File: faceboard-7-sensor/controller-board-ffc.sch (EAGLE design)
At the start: 8 parts, among them J1 DCJ0202

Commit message: redraw schematics
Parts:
- removed FACEBOARD: 52806-1410, 52806-1410:52806-1410
- RIBBON1: value 686114148922 -> (none)
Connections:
- net FRAM_CLK renamed CLK
- net FRAM_CS renamed CS
- net FRAM_MISO renamed MISO
- net FRAM_MOSI renamed MOSI
- net ROTA renamed RA
- net ROTB renamed RB
- net ROTC renamed RC
- removed net 5V: FACEBOARD.3, J1.1, RIBBON1.3, U$1.RAW
- removed net A4: FACEBOARD.12, RIBBON1.12, U$1.A4
- removed net A6: FACEBOARD.14, RIBBON1.14, U$1.A6
- removed net A7: U$1.A7
- removed net AREF: U$1.AREF
- removed net D0: U$1.TX0
- removed net D1: U$1.RX1
- removed net D13: U$1.D13
- removed net LEDDATA: FACEBOARD.7, LEDR.2, RIBBON1.7
- removed net N$8: FRAM.1
- removed net NC3V: FRAM.7
- removed net RST0: U$1.RST
- removed net VUSB: U$1.5.5V
- new net DIN: LEDR.2, RIBBON1.7
- new net N$1: RIBBON1.12, U$1.A4
- new net N$2: RIBBON1.14, U$1.A6
- new net VCC: J1.1, RIBBON1.3, U$1.RAW
- net 3V: no longer FACEBOARD.2
- net A: no longer FACEBOARD.4
- net A0: no longer FACEBOARD.8
- net A1: no longer FACEBOARD.9
- net A2: no longer FACEBOARD.10
- net A3: no longer FACEBOARD.11
- net A5: no longer FACEBOARD.13
- net B: no longer FACEBOARD.5
- net C: no longer FACEBOARD.6
- net GND: no longer FACEBOARD.1
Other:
- moved on the sheet: FRAM, J1, RESET, ROTARY

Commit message: reroute
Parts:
- RIBBON1: value (none) -> Signal
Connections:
- net N$1 renamed A4
- net N$2 renamed A6
- net A: now also U$1.D8; no longer U$1.D6
- net C: now also U$1.D6; no longer U$1.D8
- net GND: now also FRAM.7; no longer FRAM.6
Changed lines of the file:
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@@
 <part name="LEDR" library="rcl" library_urn="urn:adsk.eagle:library:334" deviceset="R-EU_" device="0207/10" package3d_urn="urn:adsk.eagle:package:23491/2" value="300"/>
 <part name="FRAM" library="con-lstb" library_urn="urn:adsk.eagle:library:162" deviceset="MA08-1" device="" package3d_urn="urn:adsk.eagle:package:8343/1" value="MB85RS2MTA"/>
-<part name="RIBBON1" library="686114148922" deviceset="686114148922" device=""/>
+<part name="RIBBON1" library="686114148922" deviceset="686114148922" device="" value="Signal"/>
 <part name="J1" library="con-jack" library_urn="urn:adsk.eagle:library:154" deviceset="DCJ0202" device="" package3d_urn="urn:adsk.eagle:package:7491/1"/>
 <part name="RESET" library="con-jst-ph" deviceset="B2B-PH-K" device=""/>
@@
 <pinref part="RIBBON1" gate="G$1" pin="13"/>
 <wire x1="38.1" y1="53.34" x2="17.018" y2="53.34" width="0.1524" layer="91"/>
+<label x="22.86" y="53.34" size="1.778" layer="95"/>
 </segment>
 </net>
@@
 </segment>
 </net>
-<net name="A0" class="0">
-<segment>
-<pinref part="U$1" gate="G$1" pin="A0"/>
-<wire x1="17.018" y1="66.04" x2="38.1" y2="66.04" width="0.1524" layer="91"/>
-<wire x1="17.018" y1="66.04" x2="17.272" y2="66.04" width="0.1524" layer="91"/>
-<pinref part="RIBBON1" gate="G$1" pin="8"/>
-</segment>
-</net>
 <net name="A" class="0">
+<segment>
+<wire x1="17.018" y1="76.2" x2="17.272" y2="76.2" width="0.1524" layer="91"/>
+<label x="17.272" y="76.2" size="1.778" layer="95" xref="yes"/>
+<pinref part="RIBBON1" gate="G$1" pin="4"/>
+</segment>
+<segment>
+<pinref part="U$1" gate="G$1" pin="D8"/>
+<wire x1="71.12" y1="63.5" x2="71.628" y2="63.5" width="0.1524" layer="91"/>
+<label x="75.692" y="63.5" size="1.778" layer="95" rot="MR0" xref="yes"/>
+</segment>
+</net>
+<net name="B" class="0">
+<segment>
+<pinref part="U$1" gate="G$1" pin="D7"/>
+<wire x1="75.692" y1="60.96" x2="71.12" y2="60.96" width="0.1524" layer="91"/>
+<label x="79.756" y="60.96" size="1.778" layer="95" rot="MR0" xref="yes"/>
+</segment>
+<segment>
+<wire x1="17.018" y1="73.66" x2="22.352" y2="73.66" width="0.1524" layer="91"/>
+<label x="22.352" y="73.66" size="1.778" layer="95" xref="yes"/>
+<pinref part="RIBBON1" gate="G$1" pin="5"/>
+</segment>
+</net>
+<net name="C" class="0">
+<segment>
+<wire x1="17.018" y1="71.12" x2="17.272" y2="71.12" width="0.1524" layer="91"/>
+<label x="17.272" y="71.12" size="1.778" layer="95" xref="yes"/>
+<pinref part="RIBBON1" gate="G$1" pin="6"/>
+</segment>
 <segment>
 <pinref part="U$1" gate="G$1" pin="D6"/>
@@
 <label x="75.438" y="58.42" size="1.778" layer="95" rot="MR0" xref="yes"/>
 </segment>
-<segment>
-<wire x1="17.018" y1="76.2" x2="17.272" y2="76.2" width="0.1524" layer="91"/>
-<label x="17.272" y="76.2" size="1.778" layer="95" xref="yes"/>
-<pinref part="RIBBON1" gate="G$1" pin="4"/>
-</segment>
-</net>
-<net name="B" class="0">
-<segment>
-<pinref part="U$1" gate="G$1" pin="D7"/>
-<wire x1="75.692" y1="60.96" x2="71.12" y2="60.96" width="0.1524" layer="91"/>
-<label x="79.756" y="60.96" size="1.778" layer="95" rot="MR0" xref="yes"/>
-</segment>
-<segment>
-<wire x1="17.018" y1="73.66" x2="22.352" y2="73.66" width="0.1524" layer="91"/>
-<label x="22.352" y="73.66" size="1.778" layer="95" xref="yes"/>
-<pinref part="RIBBON1" gate="G$1" pin="5"/>
-</segment>
-</net>
-<net name="C" class="0">
-<segment>
-<pinref part="U$1" gate="G$1" pin="D8"/>
-<wire x1="71.12" y1="63.5" x2="71.628" y2="63.5" width="0.1524" layer="91"/>
-<label x="75.692" y="63.5" size="1.778" layer="95" rot="MR0" xref="yes"/>
-</segment>
-<segment>
-<wire x1="17.018" y1="71.12" x2="17.272" y2="71.12" width="0.1524" layer="91"/>
-<label x="17.272" y="71.12" size="1.778" layer="95" xref="yes"/>
-<pinref part="RIBBON1" gate="G$1" pin="6"/>
-</segment>
 </net>
 <net name="RST" class="0">
@@
 <wire x1="39.37" y1="4.064" x2="32.766" y2="4.064" width="0.1524" layer="91"/>
 <label x="32.766" y="4.064" size="1.778" layer="95" rot="R180" xref="yes"/>
-</segment>
-<segment>
-<wire x1="69.85" y1="9.906" x2="70.104" y2="9.906" width="0.1524" layer="91"/>
-<pinref part="FRAM" gate="1" pin="6"/>
-<label x="70.104" y="9.906" size="1.778" layer="95" rot="MR180" xref="yes"/>
 </segment>
 <segment>
@@
 <wire x1="27.94" y1="43.18" x2="27.94" y2="40.64" width="0.1524" layer="91"/>
 <junction x="27.94" y="40.64"/>
+<label x="33.02" y="40.64" size="1.778" layer="95" rot="R90" xref="yes"/>
+</segment>
+<segment>
+<pinref part="FRAM" gate="1" pin="7"/>
+<wire x1="69.85" y1="7.366" x2="76.2" y2="7.366" width="0.1524" layer="91"/>
+<label x="76.454" y="7.366" size="1.778" layer="95" xref="yes"/>
 </segment>
 </net>
@@
 </segment>
 </net>
-<net name="N$1" class="0">
+<net name="A4" class="0">
 <segment>
 <pinref part="U$1" gate="G$1" pin="A4"/>
 <pinref part="RIBBON1" gate="G$1" pin="12"/>
 <wire x1="38.1" y1="55.88" x2="17.018" y2="55.88" width="0.1524" layer="91"/>
-</segment>
-</net>
-<net name="N$2" class="0">
+<label x="22.86" y="55.88" size="1.778" layer="95"/>
+</segment>
+</net>
+<net name="A6" class="0">
 <segment>
 <pinref part="U$1" gate="G$1" pin="A6"/>
 <pinref part="RIBBON1" gate="G$1" pin="14"/>
 <wire x1="38.1" y1="50.8" x2="17.018" y2="50.8" width="0.1524" layer="91"/>
-</segment>
-</net>
+<label x="22.86" y="50.8" size="1.778" layer="95"/>
+</segment>
+</net>
+<net name="A0" class="0">
+<segment>
+<pinref part="RIBBON1" gate="G$1" pin="8"/>
+<pinref part="U$1" gate="G$1" pin="A0"/>
+<wire x1="17.018" y1="66.04" x2="38.1" y2="66.04" width="0.1524" layer="91"/>
+<label x="30.48" y="66.04" size="1.778" layer="95" rot="R90" xref="yes"/>
+</segment>
+</net>

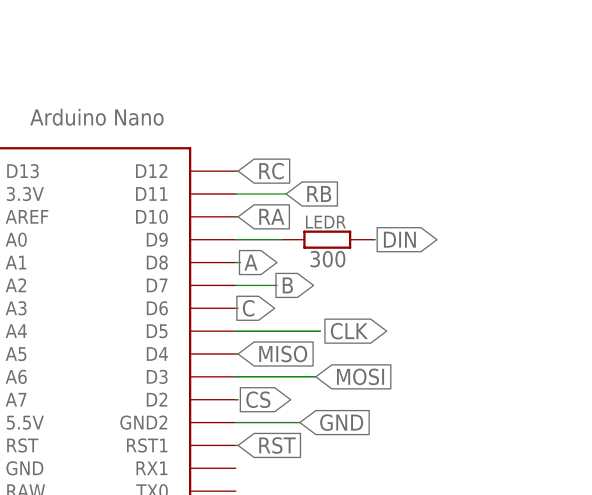
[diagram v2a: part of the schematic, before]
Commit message: tidy silk screen
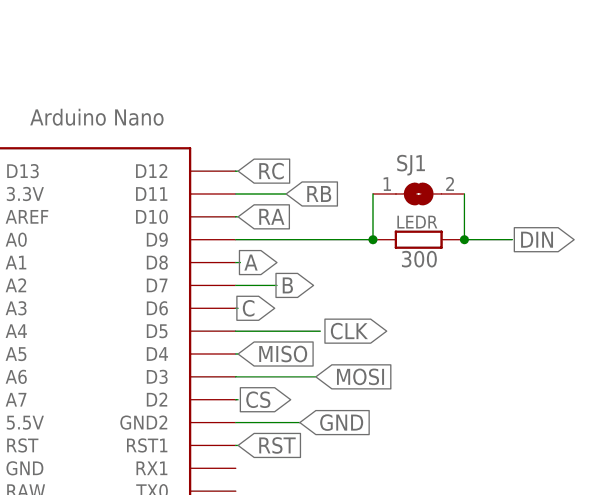
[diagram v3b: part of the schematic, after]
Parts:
- added SJ1: (no value), jumper:SJ
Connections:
- net D9: now also SJ1.1
- net DIN: now also SJ1.2
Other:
- moved on the sheet: LEDR
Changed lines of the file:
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@@
 <part name="RESET" library="con-jst-ph" deviceset="B2B-PH-K" device=""/>
 <part name="GND1" library="supply1" library_urn="urn:adsk.eagle:library:371" deviceset="GND" device=""/>
+<part name="SJ1" library="jumper" library_urn="urn:adsk.eagle:library:252" deviceset="SJ" device="" package3d_urn="urn:adsk.eagle:package:15471/1"/>
 </parts>
 <sheets>
@@
 <attribute name="NAME" x="50.419" y="12.954" size="1.778" layer="95" rot="R90"/>
 </instance>
-<instance part="LEDR" gate="G$1" x="81.28" y="66.04" smashed="yes">
-<attribute name="NAME" x="78.74" y="67.2846" size="1.4224" layer="95"/>
-<attribute name="VALUE" x="79.248" y="62.992" size="1.778" layer="96"/>
+<instance part="LEDR" gate="G$1" x="91.44" y="66.04" smashed="yes">
+<attribute name="NAME" x="88.9" y="67.2846" size="1.4224" layer="95"/>
+<attribute name="VALUE" x="89.408" y="62.992" size="1.778" layer="96"/>
 </instance>
 <instance part="FRAM" gate="1" x="62.23" y="14.986" smashed="yes" rot="MR180">
@@
 <instance part="GND1" gate="1" x="-8.382" y="75.184" smashed="yes">
 <attribute name="VALUE" x="-10.922" y="72.644" size="1.778" layer="96"/>
+</instance>
+<instance part="SJ1" gate="1" x="91.44" y="71.12" smashed="yes">
+<attribute name="NAME" x="88.9" y="73.66" size="1.778" layer="95"/>
+<attribute name="VALUE" x="88.9" y="67.31" size="1.778" layer="96"/>
 </instance>
 </instances>
@@
 <net name="DIN" class="0">
 <segment>
-<wire x1="86.614" y1="66.04" x2="86.36" y2="66.04" width="0.1524" layer="91"/>
-<label x="93.472" y="66.04" size="1.778" layer="95" rot="R180" xref="yes"/>
+<wire x1="101.854" y1="66.04" x2="96.52" y2="66.04" width="0.1524" layer="91"/>
+<label x="108.712" y="66.04" size="1.778" layer="95" rot="R180" xref="yes"/>
 <pinref part="LEDR" gate="G$1" pin="2"/>
+<pinref part="SJ1" gate="1" pin="2"/>
+<wire x1="96.52" y1="71.12" x2="96.52" y2="66.04" width="0.1524" layer="91"/>
+<junction x="96.52" y="66.04"/>
 </segment>
 <segment>
@@
 <pinref part="U$1" gate="G$1" pin="D9"/>
 <pinref part="LEDR" gate="G$1" pin="1"/>
-<wire x1="76.2" y1="66.04" x2="71.12" y2="66.04" width="0.1524" layer="91"/>
-</segment>
-</net>
+<wire x1="86.36" y1="66.04" x2="71.12" y2="66.04" width="0.1524" layer="91"/>
+<pinref part="SJ1" gate="1" pin="1"/>
+<wire x1="86.36" y1="66.04" x2="86.36" y2="71.12" width="0.1524" layer="91"/>
+<junction x="86.36" y="66.04"/>
+</segment>
+</net>
